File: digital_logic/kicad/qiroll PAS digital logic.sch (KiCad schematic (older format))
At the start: 13 parts, among them U1 14538, U2 4023, U3 4027, U4 14538

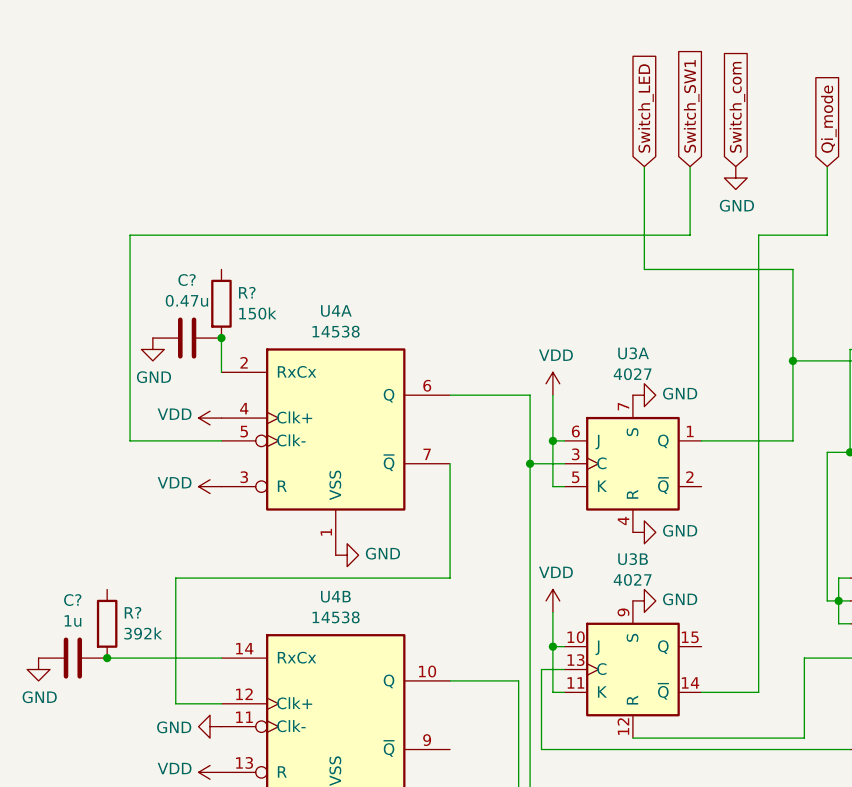
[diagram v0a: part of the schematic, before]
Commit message: fix schematic, export to png
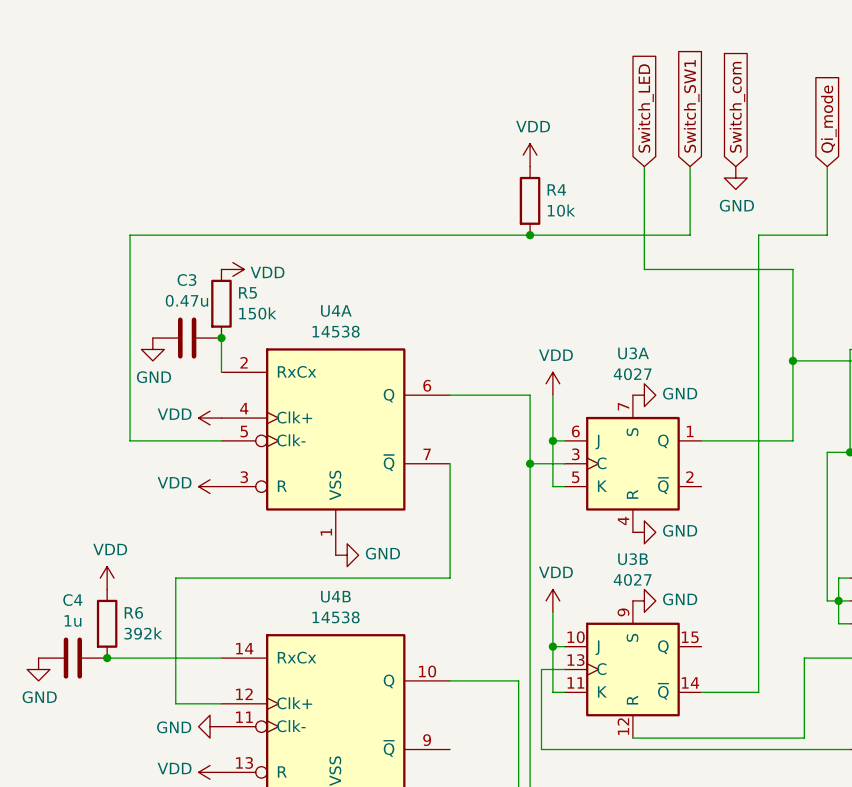
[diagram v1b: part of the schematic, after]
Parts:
- added R4: 10k, symbol Device:R
- gave numbers to parts that had none: 4
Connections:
- net Switch_SW1: now also R4.2
- net VDD: now also R5.1, R6.1, R4.1
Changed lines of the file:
@@
 	2850 2700 3250 2700
 Wire Wire Line
-	2850 1800 5300 1800
+	2850 1800 4600 1800
 $Comp
 L power:VDD #PWR?
@@
 	4550 3750 4250 3750
 $Comp
-L Device:R R?
+L Device:R R5
 U 1 1 6038DA08
 P 3250 2100
-F 0 "R?" H 3320 2146 50  0000 L CNN
+F 0 "R5" H 3320 2146 50  0000 L CNN
 F 1 "150k" H 3320 2055 50  0000 L CNN
 F 2 "" V 3180 2100 50  0001 C CNN
@@
 $EndComp
 $Comp
-L Device:C C?
+L Device:C C3
 U 1 1 6038DA16
 P 3100 2250
-F 0 "C?" V 2848 2250 50  0000 C CNN
+F 0 "C3" V 2848 2250 50  0000 C CNN
 F 1 "0.47u" V 2939 2250 50  0000 C CNN
 F 2 "" H 3138 2100 50  0001 C CNN
@@
 $EndComp
 $Comp
-L Device:R R?
+L Device:R R6
 U 1 1 60394144
 P 2750 3500
-F 0 "R?" H 2820 3546 50  0000 L CNN
+F 0 "R6" H 2820 3546 50  0000 L CNN
 F 1 "392k" H 2820 3455 50  0000 L CNN
 F 2 "" V 2680 3500 50  0001 C CNN
@@
 $EndComp
 $Comp
-L Device:C C?
+L Device:C C4
 U 1 1 60394152
 P 2600 3650
-F 0 "C?" V 2348 3650 50  0000 C CNN
+F 0 "C4" V 2348 3650 50  0000 C CNN
 F 1 "1u" V 2439 3650 50  0000 C CNN
 F 2 "" H 2638 3500 50  0001 C CNN
@@
 Wire Wire Line
 	2750 3650 3250 3650
+$Comp
+L Device:R R4
+U 1 1 603A1239
+P 4600 1650
+F 0 "R4" H 4670 1696 50  0000 L CNN
+F 1 "10k" H 4670 1605 50  0000 L CNN
+F 2 "" V 4530 1650 50  0001 C CNN
+F 3 "~" H 4600 1650 50  0001 C CNN
+	1    4600 1650
+	1    0    0    -1
+$EndComp
+Connection ~ 4600 1800
+Wire Wire Line
+	4600 1800 5300 1800
+$Comp
+L power:VDD #PWR?
+U 1 1 6032C2BA
+P 4600 1500
+F 0 "#PWR?" H 4600 1350 50  0001 C CNN
+F 1 "VDD" H 4615 1673 50  0000 C CNN
+F 2 "" H 4600 1500 50  0001 C CNN
+F 3 "" H 4600 1500 50  0001 C CNN
+	1    4600 1500
+	1    0    0    -1
+$EndComp
+$Comp
+L power:VDD #PWR?
+U 1 1 6032F19D
+P 2750 3350
+F 0 "#PWR?" H 2750 3200 50  0001 C CNN
+F 1 "VDD" H 2765 3523 50  0000 C CNN
+F 2 "" H 2750 3350 50  0001 C CNN
+F 3 "" H 2750 3350 50  0001 C CNN
+	1    2750 3350
+	1    0    0    -1
+$EndComp
+$Comp
+L power:VDD #PWR?
+U 1 1 6032E2B8
+P 3250 1950
+F 0 "#PWR?" H 3250 1800 50  0001 C CNN
+F 1 "VDD" V 3265 2077 50  0000 L CNN
+F 2 "" H 3250 1950 50  0001 C CNN
+F 3 "" H 3250 1950 50  0001 C CNN
+	1    3250 1950
+	0    1    1    0
+$EndComp
 $EndSCHEMATC

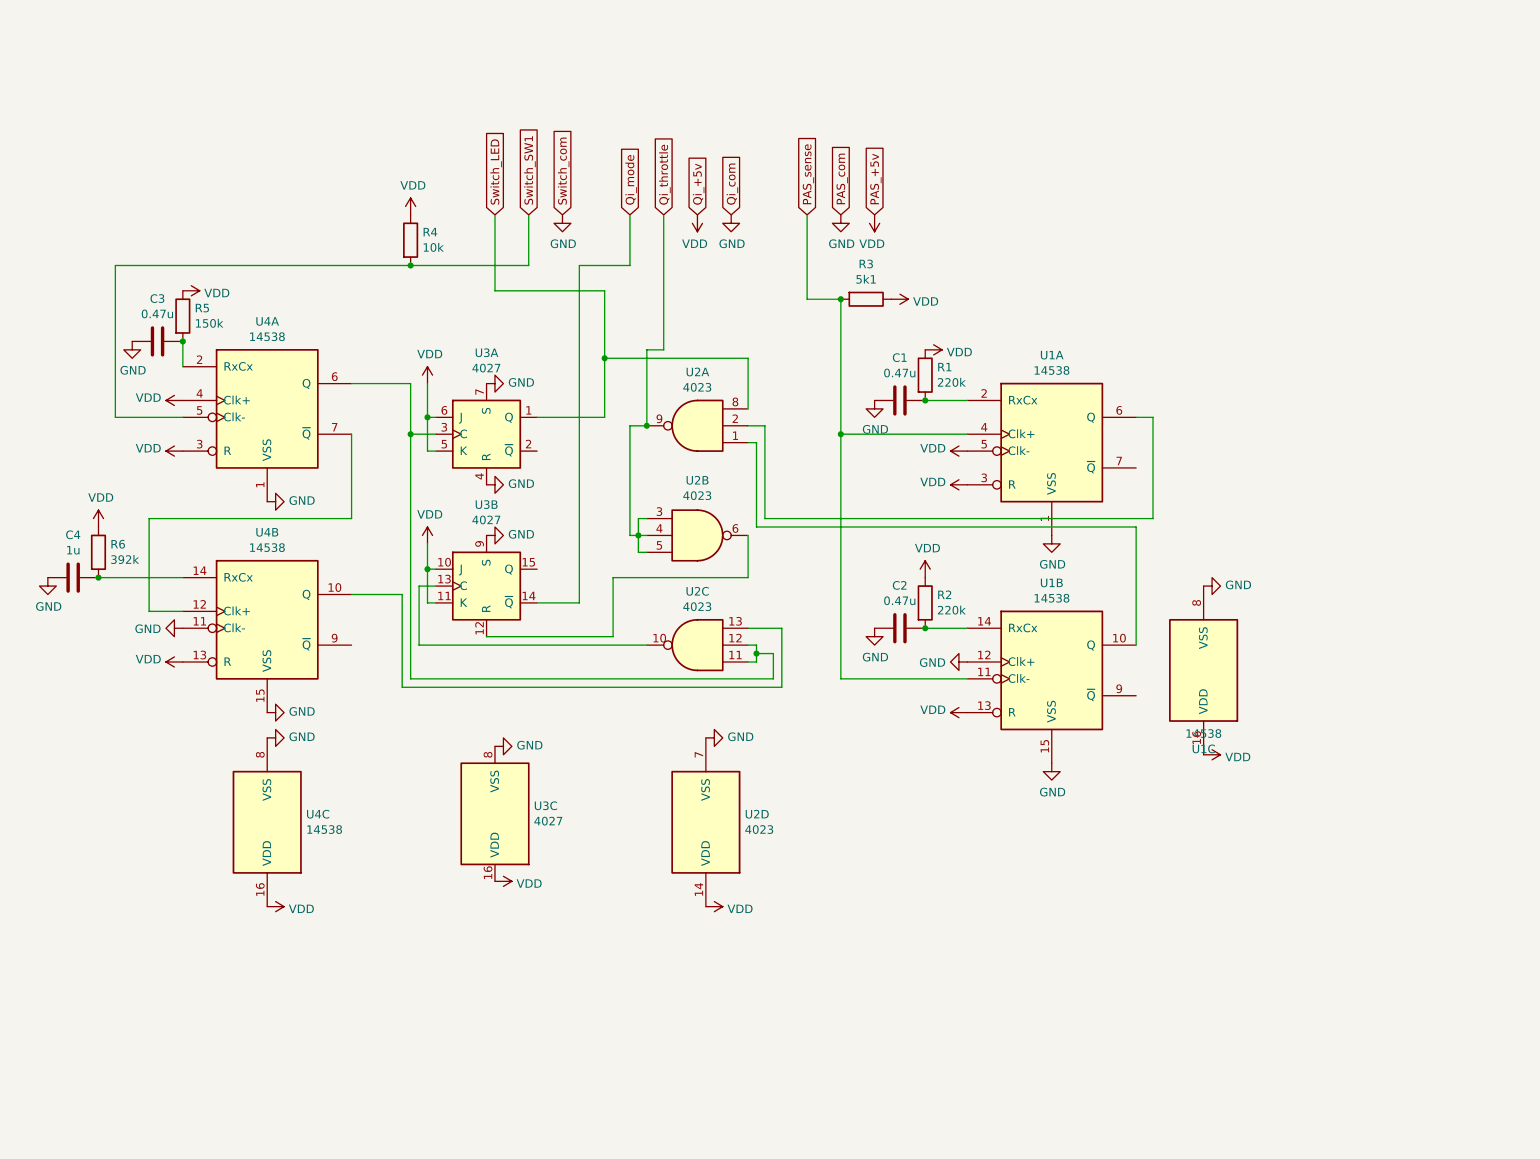
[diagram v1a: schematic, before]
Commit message: add rc debounce, decoupling
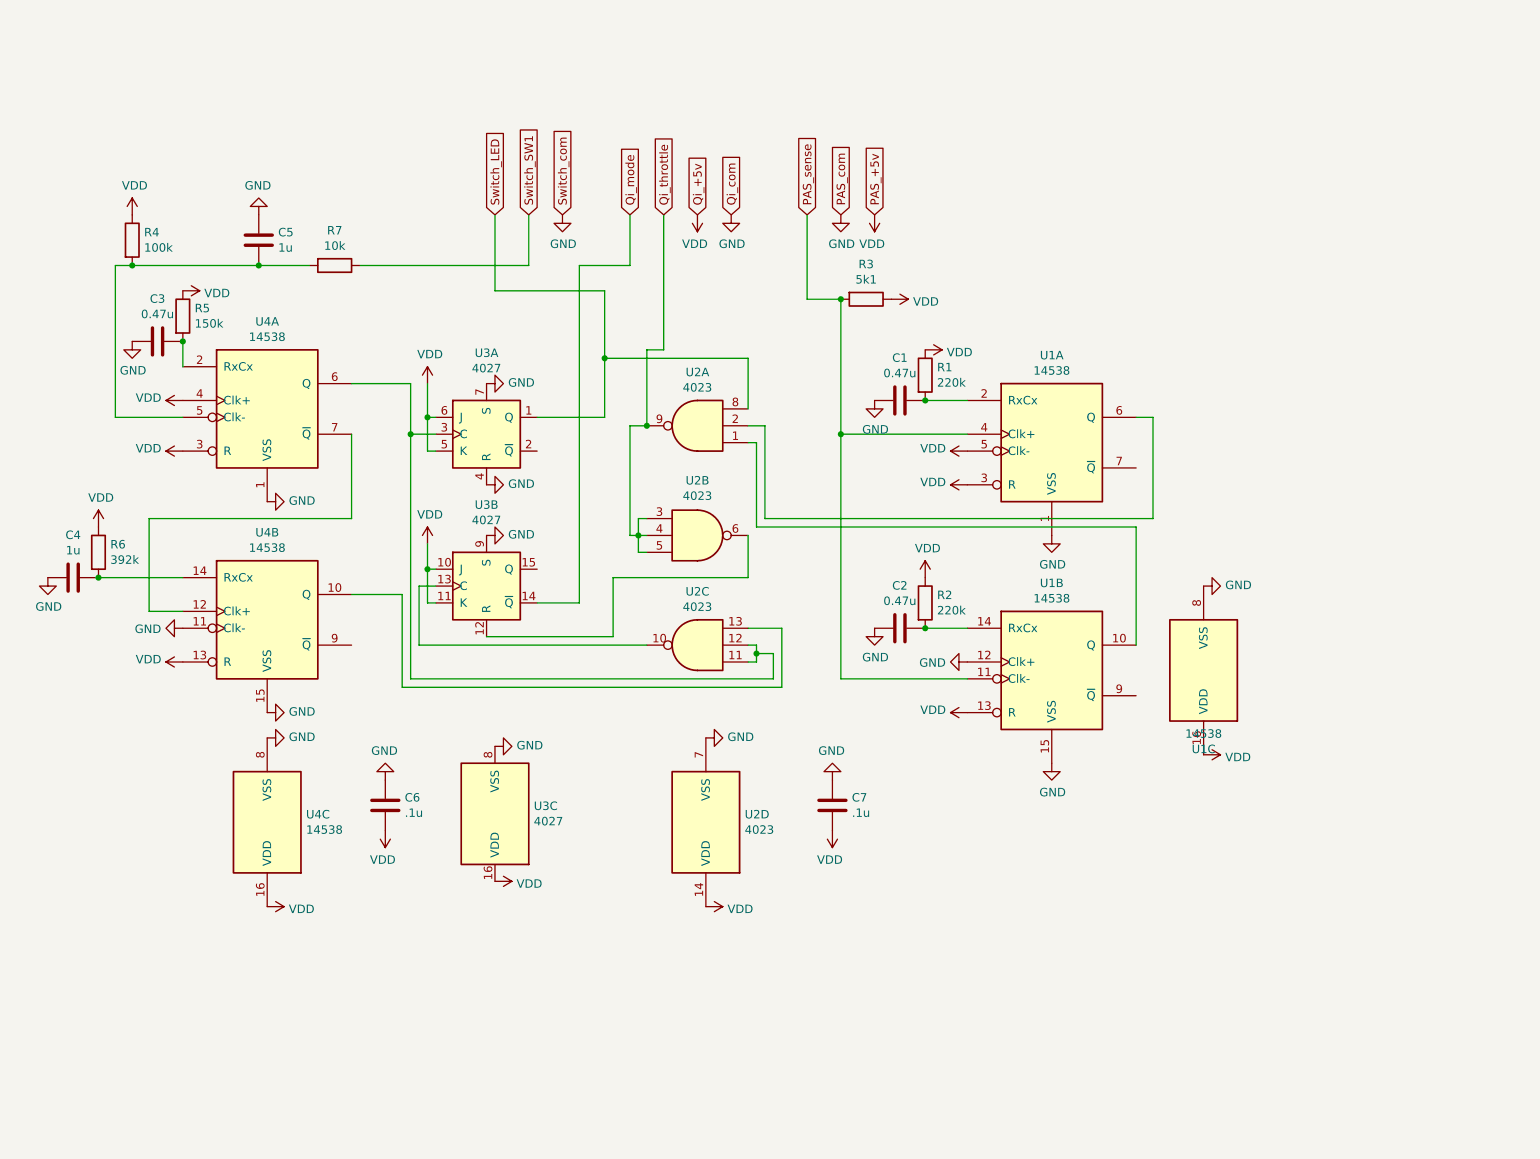
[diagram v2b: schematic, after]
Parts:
- added C5: 1u, symbol Device:C
- added C6, C7: .1u, symbol Device:C
- added R7: 10k, symbol Device:R
- R4: value 10k -> 100k
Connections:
- net GND: now also C5.1, C6.1, C7.1
- net Switch_SW1: now also R7.1; no longer R4.2, U4.5 (Clk-)
- net VDD: now also C6.2, C7.2
- new net: C5.2, R4.2, R7.2, U4.5 (Clk-)
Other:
- moved on the sheet: R4
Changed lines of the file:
@@
 	2850 2700 3250 2700
 Wire Wire Line
-	2850 1800 4600 1800
+	2850 1800 2950 1800
 $Comp
 L power:VDD #PWR?
@@
 L Device:R R4
 U 1 1 603A1239
-P 4600 1650
-F 0 "R4" H 4670 1696 50  0000 L CNN
-F 1 "10k" H 4670 1605 50  0000 L CNN
-F 2 "" V 4530 1650 50  0001 C CNN
-F 3 "~" H 4600 1650 50  0001 C CNN
-	1    4600 1650
-	1    0    0    -1
-$EndComp
-Connection ~ 4600 1800
-Wire Wire Line
-	4600 1800 5300 1800
+P 2950 1650
+F 0 "R4" H 3020 1696 50  0000 L CNN
+F 1 "100k" H 3020 1605 50  0000 L CNN
+F 2 "" V 2880 1650 50  0001 C CNN
+F 3 "~" H 2950 1650 50  0001 C CNN
+	1    2950 1650
+	1    0    0    -1
+$EndComp
 $Comp
 L power:VDD #PWR?
 U 1 1 6032C2BA
-P 4600 1500
-F 0 "#PWR?" H 4600 1350 50  0001 C CNN
-F 1 "VDD" H 4615 1673 50  0000 C CNN
-F 2 "" H 4600 1500 50  0001 C CNN
-F 3 "" H 4600 1500 50  0001 C CNN
-	1    4600 1500
+P 2950 1500
+F 0 "#PWR?" H 2950 1350 50  0001 C CNN
+F 1 "VDD" H 2965 1673 50  0000 C CNN
+F 2 "" H 2950 1500 50  0001 C CNN
+F 3 "" H 2950 1500 50  0001 C CNN
+	1    2950 1500
 	1    0    0    -1
 $EndComp
@@
 	0    1    1    0
 $EndComp
+$Comp
+L Device:R R7
+U 1 1 6061C755
+P 4150 1800
+F 0 "R7" V 3943 1800 50  0000 C CNN
+F 1 "10k" V 4034 1800 50  0000 C CNN
+F 2 "" V 4080 1800 50  0001 C CNN
+F 3 "~" H 4150 1800 50  0001 C CNN
+	1    4150 1800
+	0    1    1    0
+$EndComp
+$Comp
+L Device:C C5
+U 1 1 6061DDAE
+P 3700 1650
+F 0 "C5" H 3815 1696 50  0000 L CNN
+F 1 "1u" H 3815 1605 50  0000 L CNN
+F 2 "" H 3738 1500 50  0001 C CNN
+F 3 "~" H 3700 1650 50  0001 C CNN
+	1    3700 1650
+	1    0    0    -1
+$EndComp
+Wire Wire Line
+	2950 1800 3700 1800
+Connection ~ 2950 1800
+Wire Wire Line
+	3700 1800 4000 1800
+Connection ~ 3700 1800
+Wire Wire Line
+	4300 1800 5300 1800
+$Comp
+L power:GND #PWR?
+U 1 1 6062B8A2
+P 3700 1500
+F 0 "#PWR?" H 3700 1250 50  0001 C CNN
+F 1 "GND" H 3705 1327 50  0000 C CNN
+F 2 "" H 3700 1500 50  0001 C CNN
+F 3 "" H 3700 1500 50  0001 C CNN
+	1    3700 1500
+	-1   0    0    1
+$EndComp
+$Comp
+L Device:C C6
+U 1 1 6062C108
+P 4450 5000
+F 0 "C6" H 4565 5046 50  0000 L CNN
+F 1 ".1u" H 4565 4955 50  0000 L CNN
+F 2 "" H 4488 4850 50  0001 C CNN
+F 3 "~" H 4450 5000 50  0001 C CNN
+	1    4450 5000
+	1    0    0    -1
+$EndComp
+$Comp
+L power:GND #PWR?
+U 1 1 6062D54C
+P 4450 4850
+F 0 "#PWR?" H 4450 4600 50  0001 C CNN
+F 1 "GND" H 4455 4677 50  0000 C CNN
+F 2 "" H 4450 4850 50  0001 C CNN
+F 3 "" H 4450 4850 50  0001 C CNN
+	1    4450 4850
+	-1   0    0    1
+$EndComp
+$Comp
+L power:VDD #PWR?
+U 1 1 6062DF28
+P 4450 5150
+F 0 "#PWR?" H 4450 5000 50  0001 C CNN
+F 1 "VDD" H 4465 5323 50  0000 C CNN
+F 2 "" H 4450 5150 50  0001 C CNN
+F 3 "" H 4450 5150 50  0001 C CNN
+	1    4450 5150
+	-1   0    0    1
+$EndComp
+$Comp
+L Device:C C7
+U 1 1 6062E968
+P 7100 5000
+F 0 "C7" H 7215 5046 50  0000 L CNN
+F 1 ".1u" H 7215 4955 50  0000 L CNN
+F 2 "" H 7138 4850 50  0001 C CNN
+F 3 "~" H 7100 5000 50  0001 C CNN
+	1    7100 5000
+	1    0    0    -1
+$EndComp
+$Comp
+L power:GND #PWR?
+U 1 1 6062E96E
+P 7100 4850
+F 0 "#PWR?" H 7100 4600 50  0001 C CNN
+F 1 "GND" H 7105 4677 50  0000 C CNN
+F 2 "" H 7100 4850 50  0001 C CNN
+F 3 "" H 7100 4850 50  0001 C CNN
+	1    7100 4850
+	-1   0    0    1
+$EndComp
+$Comp
+L power:VDD #PWR?
+U 1 1 6062E974
+P 7100 5150
+F 0 "#PWR?" H 7100 5000 50  0001 C CNN
+F 1 "VDD" H 7115 5323 50  0000 C CNN
+F 2 "" H 7100 5150 50  0001 C CNN
+F 3 "" H 7100 5150 50  0001 C CNN
+	1    7100 5150
+	-1   0    0    1
+$EndComp
 $EndSCHEMATC

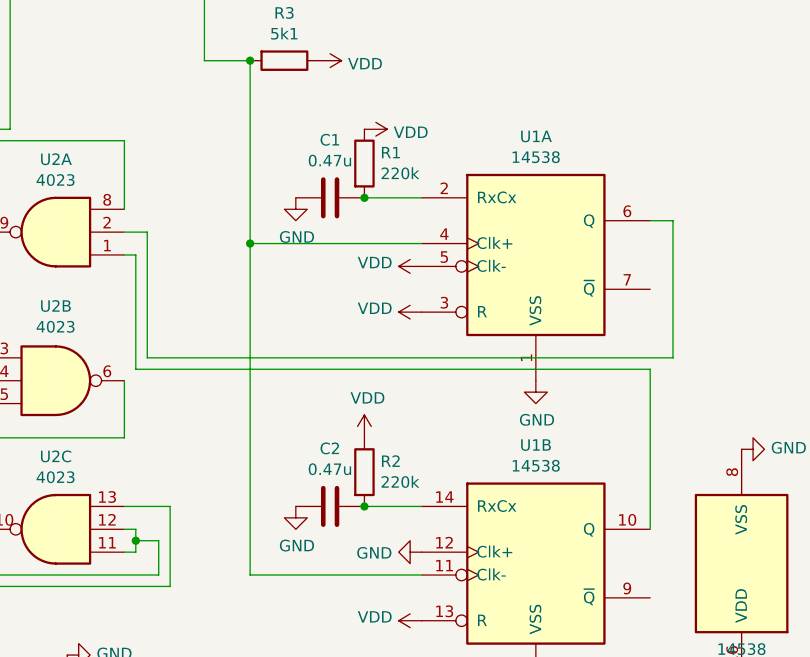
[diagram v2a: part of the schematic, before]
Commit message: update r1r2 values
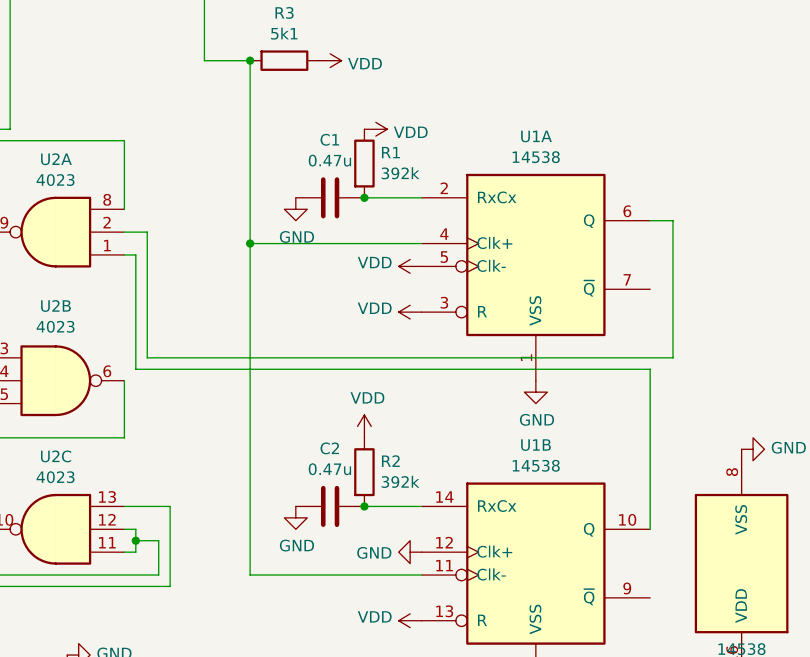
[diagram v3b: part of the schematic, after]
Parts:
- R1, R2: value 220k -> 392k
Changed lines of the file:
@@
 P 7650 2450
 F 0 "R1" H 7720 2496 50  0000 L CNN
-F 1 "220k" H 7720 2405 50  0000 L CNN
+F 1 "392k" H 7720 2405 50  0000 L CNN
 F 2 "" V 7580 2450 50  0001 C CNN
 F 3 "~" H 7650 2450 50  0001 C CNN
@@
 P 7650 3800
 F 0 "R2" H 7720 3846 50  0000 L CNN
-F 1 "220k" H 7720 3755 50  0000 L CNN
+F 1 "392k" H 7720 3755 50  0000 L CNN
 F 2 "" V 7580 3800 50  0001 C CNN
 F 3 "~" H 7650 3800 50  0001 C CNN
